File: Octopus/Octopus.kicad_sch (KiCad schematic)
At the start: 88 parts, among them J1 MIDI IN (to panel DIN), J10 RN112BPC, J11 Button panel, J2 9-12VDC IN, J3 RN112BPC, J4 RN112BPC, J5 RN112BPC, J6 RN112BPC, J7 RN112BPC, J8 RN112BPC, J9 RN112BPC, K1 G5V-1, K10 G5V-1, K11 G5V-1, K12 G5V-1, K13 G5V-1, K14 G5V-1, K15 G5V-1, K16 G5V-1, K2 G5V-1, K3 G5V-1, K4 G5V-1, K5 G5V-1, K6 G5V-1, K7 G5V-1, K8 G5V-1, K9 G5V-1, U1 Teensy4.1, U2 6N138, U3 ULN2803A, U4 R-78E5.0-1.0, U5 ULN2803A

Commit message: Octopus: MIDI THRU, FM6725 DIN sockets, SnapMagic RN112BPC parts
- MIDI IN and a hardware MIDI THRU on two Cliff FM6725 right-angle DIN
  sockets through the back panel. THRU is buffered from the opto output
  by a 74HCT14 (two gates in series) into the standard 220R/220R 5 V
  source, independent of the firmware.
- Back panel re-planned around the sockets: jacks at 0.700" pitch, DIN
  holes beside jack 1, cord hole moved 3.67 mm; hole table in README.
- FM6725 footprint generated from the Cliff datasheet (tools/gen_din_fp.py)
  with the supplied 3D model.
- Jacks now use SnapMagic's RN112BPC symbol/footprint/3D model from
  case/RN112BPC via the project library tables (the vendor files are
  git-ignored: their licence doesn't allow redistribution).
- Mains PSU keep-free zone moved to the front right; jack 8's relays
  moved below the rear-post notch with a locked hand-routed tip run.
- ERC 0 errors; DRC 0 errors, 0 unconnected, 0 parity issues (16
  vendor silkscreen-at-edge warnings).

Co-Authored-By: Claude Opus 5.5 <noreply@anthropic.com>
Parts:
- added C3: 100n, Capacitor_THT:C_Disc_D5.0mm_W2.5mm_P5.00mm, symbol Device:C
- added J12: FM6725 MIDI THRU, Octopus:DIN-5_180deg_Cliff_FM6725_Horizontal, symbol Connector:DIN-5_180degree
- added R3, R4: 220, Resistor_THT:R_Axial_DIN0207_L6.3mm_D2.5mm_P10.16mm_Horizontal, symbol Device:R
- added U6: 74HCT14, Package_DIP:DIP-14_W7.62mm, symbol 74xx:74HC14
- J1: value MIDI IN (to panel DIN) -> FM6725 MIDI IN; footprint Connector_JST:JST_XH_B5B-XH-A_1x05_P2.50mm_Vertical -> Octopus:DIN-5_180deg_Cliff_FM6725_Horizontal; symbol Connector:DIN-5 -> Connector:DIN-5_180degree
- J10, J3, J4, J5, J6, J7, J8, J9: footprint Octopus:Jack_6.35mm_Switchcraft_RN112BPC_Horizontal -> RN112BPC:SWITCHCRAFT_RN112BPC; symbol Connector_Audio:AudioJack3 -> RN112BPC:RN112BPC
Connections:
- net +5V: now also C3.1, R3.1, U6.14 (VCC)
- net GND: now also C3.2, J12.2, U6.11, U6.13, U6.5, U6.7 (GND), U6.9
- net OPTO_A: now reaches D1.1 (K), R1.2, U2.2 (C1)
- net OPTO_K: now reaches D1.2 (A), J1.5, U2.3 (C2)
- net MIDI_RX: now reaches R2.2, U1.0 (RX1), U2.6 (VO2)
- net MIDI_RX: now also U6.1
- net MIDI_IN_4: now reaches J1.4, R1.1
- new net THRU_N: U6.2, U6.3
- new net THRU_SINK: J12.5, R4.2
- new net THRU_SRC: J12.4, R3.2
- new net THRU_TX: R4.1, U6.4
- no-connect marks 4 -> 10

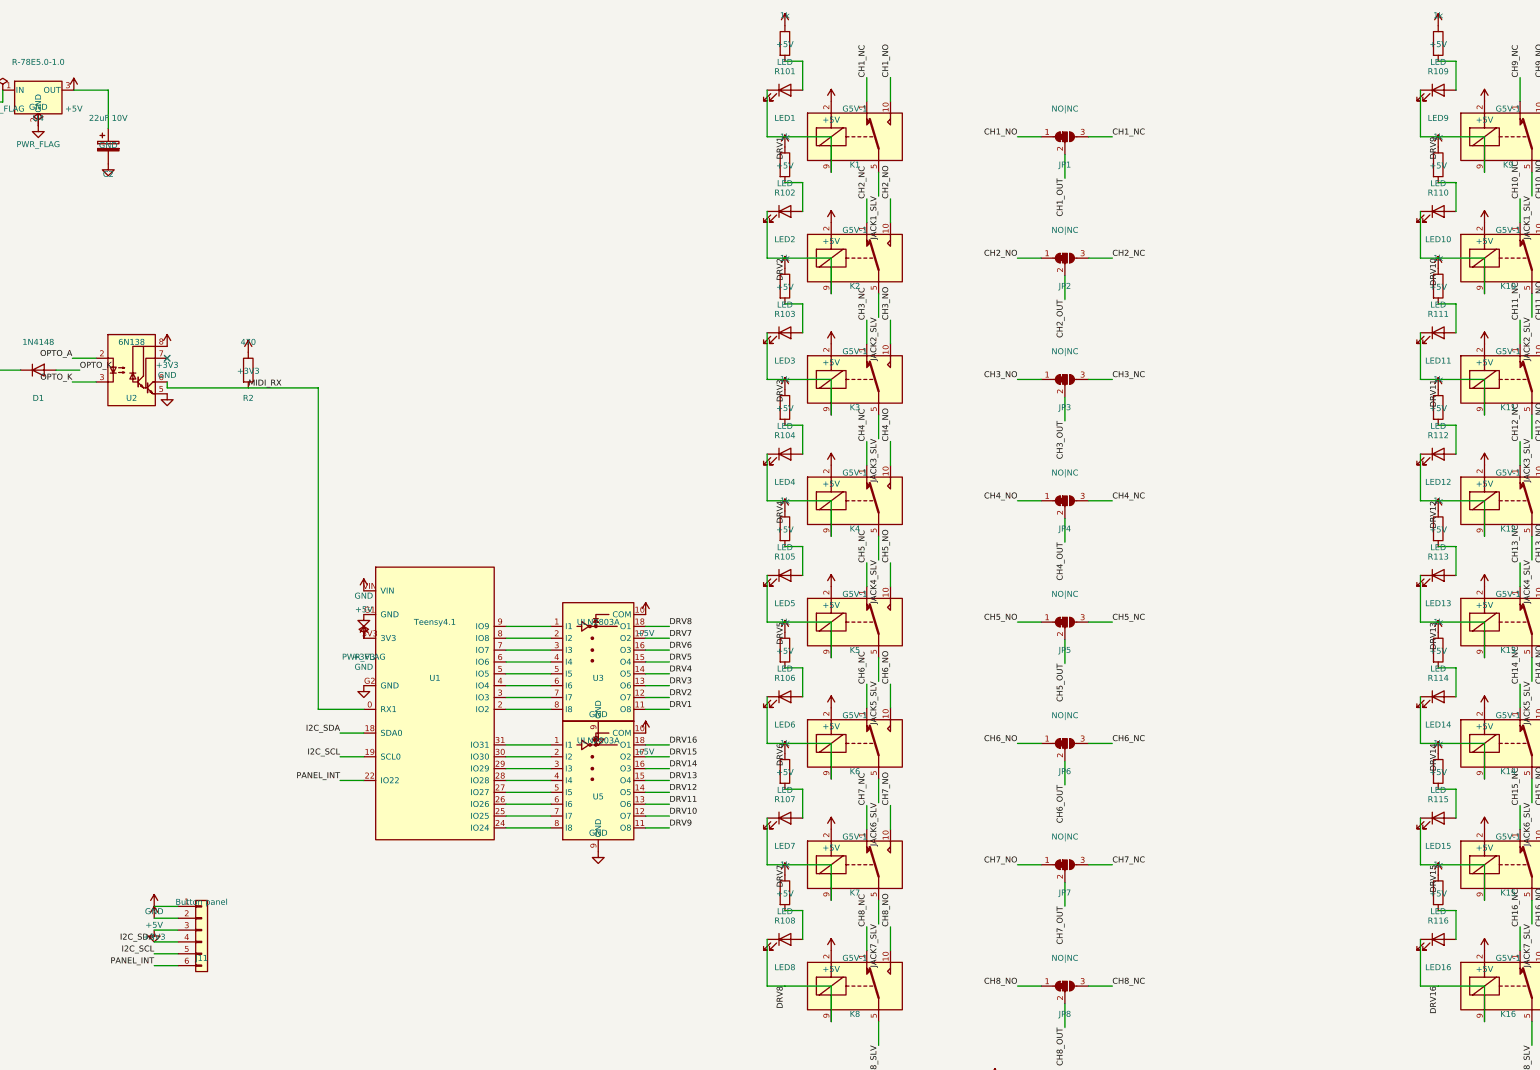
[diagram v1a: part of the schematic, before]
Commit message: Octopus: front-panel display + encoder, Omron B3W-9 buttons, DigiKey BOM
- Button board: 0.96" SSD1306 OLED (Winstar WEA012864D-03 on 5 mm
  spacers) and an Alps EC11E15204A3 encoder with push switch, left of
  the buttons. MCP23008 -> MCP23017 for the extra inputs (GPA7/GPB7
  unused: output-only on current silicon).
- Buttons: the discontinued CTS 228C RGB switches are replaced by Omron
  B3W-9000-RG2N (red + green LEDs): red = tip, green = ring, amber =
  both. One PCA9685 instead of two; LED resistors are four Bourns CAT16
  4-resistor arrays. Square 10.6 mm panel cut-outs.
- Firmware: Display (U8g2/U8x8, redraws only what changed), encoder
  decoding from the MCP23017 interrupt (half-cycle detents), SELECT? /
  push-to-load / 5 s timeout, presets shown and entered as 1-128,
  MidiHandler::recall(), bigger Serial1 RX buffer.
- Main board: status LEDs and their resistors removed (the buttons show
  every line); C2 value corrected to 22 uF 16 V.
- BOM_DigiKey.csv: full parts list by manufacturer part number
  (force-added: the repo ignores *.csv).
- ERC 0 errors on both boards; DRC 0 errors, 0 unconnected, 0 parity
  (main board: 16 vendor-footprint silkscreen-at-edge warnings).

Co-Authored-By: Claude Opus 5.5 <noreply@anthropic.com>
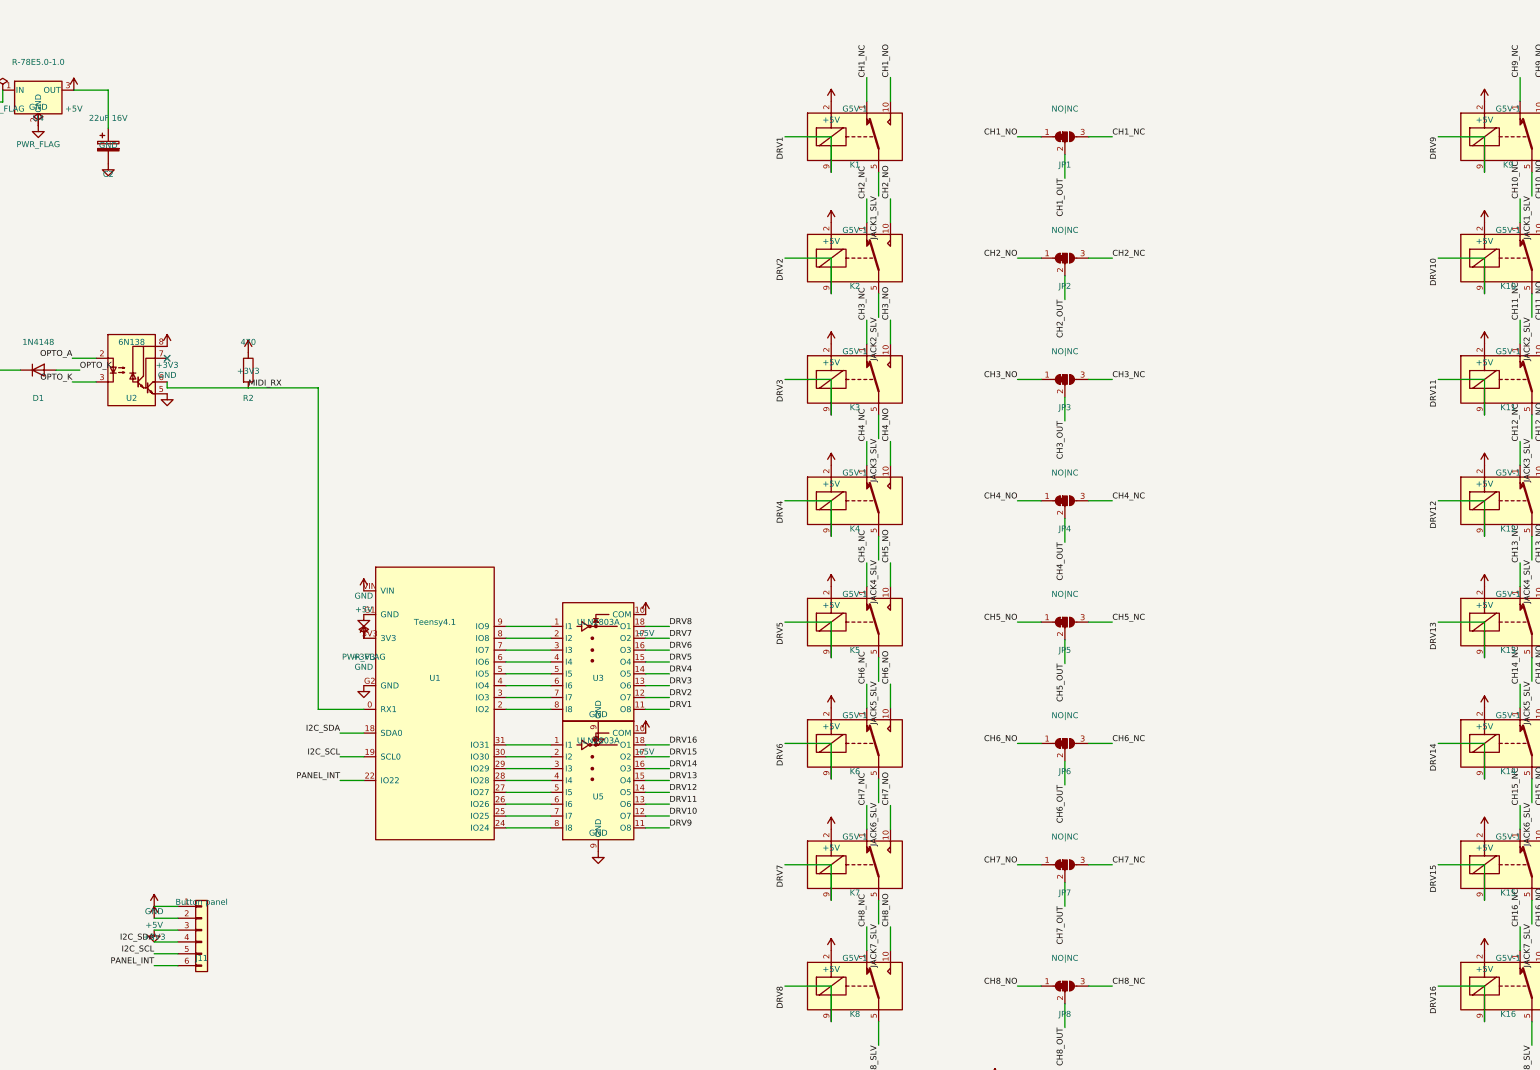
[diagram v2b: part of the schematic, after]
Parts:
- removed LED1, LED10, LED11, LED12, LED13, LED14, LED15, LED16, LED2, LED3, LED4, LED5, LED6, LED7, LED8, LED9: LED, LED_THT:LED_D3.0mm, symbol Device:LED
- removed R101, R102, R103, R104, R105, R106, R107, R108, R109, R110, R111, R112, R113, R114, R115, R116: 1k, Resistor_THT:R_Axial_DIN0207_L6.3mm_D2.5mm_P2.54mm_Vertical, symbol Device:R
- C2: value 22uF 10V -> 22uF 16V
